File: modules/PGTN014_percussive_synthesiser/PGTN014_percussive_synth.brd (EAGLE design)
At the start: 78.9 x 100.4 mm, 201 parts, among them IC1 LM13700N, IC2 LM13700N, IC3 LM13700N, IC4 4046N, IC5 XR-2206, IC6 TL074P, Q1 2N3904, Q10 2N3906, Q11 2N3906, Q12 2N3906, Q13 2N3906, Q14 2N3906, Q2 2N3904, Q3 2N3904, Q4 2N3904, Q5 2N3904, Q6 2N3904, Q7 2N3904, Q8 2N3906, Q9 2N3904

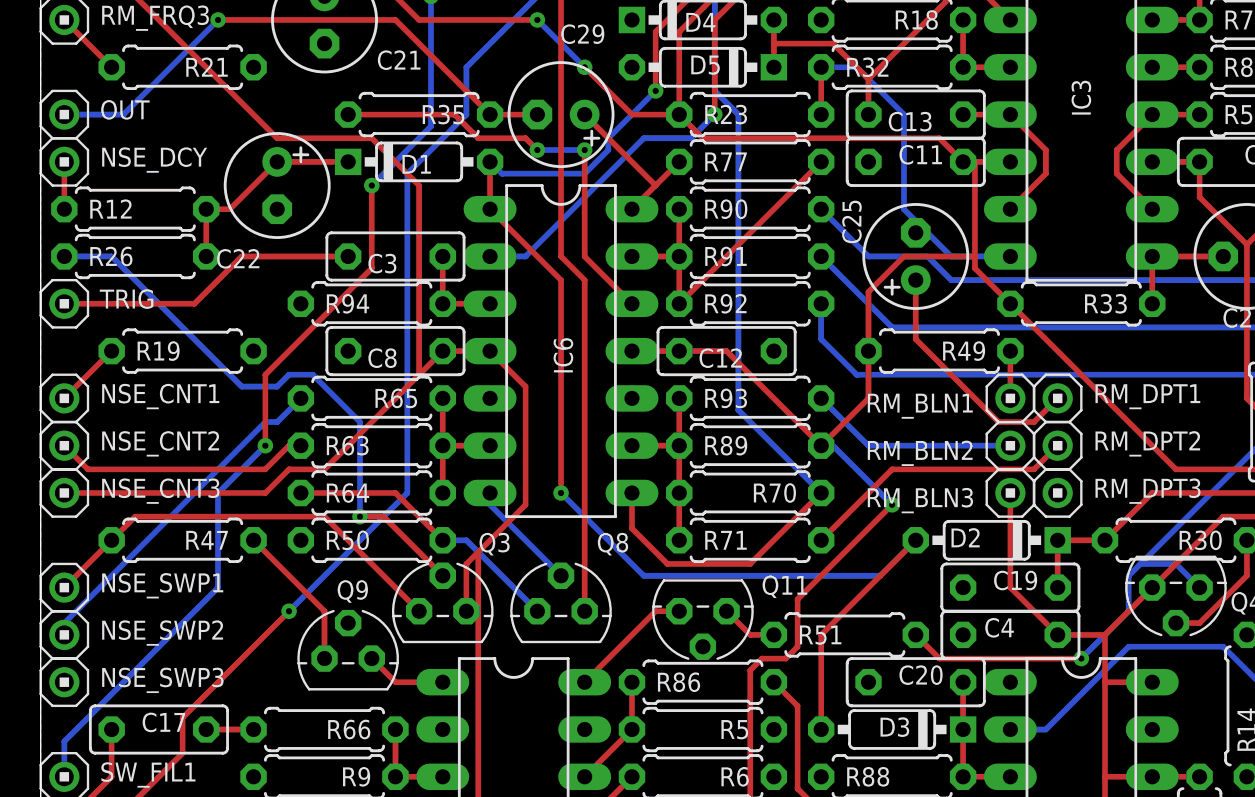
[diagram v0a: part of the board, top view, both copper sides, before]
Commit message: added sequencer
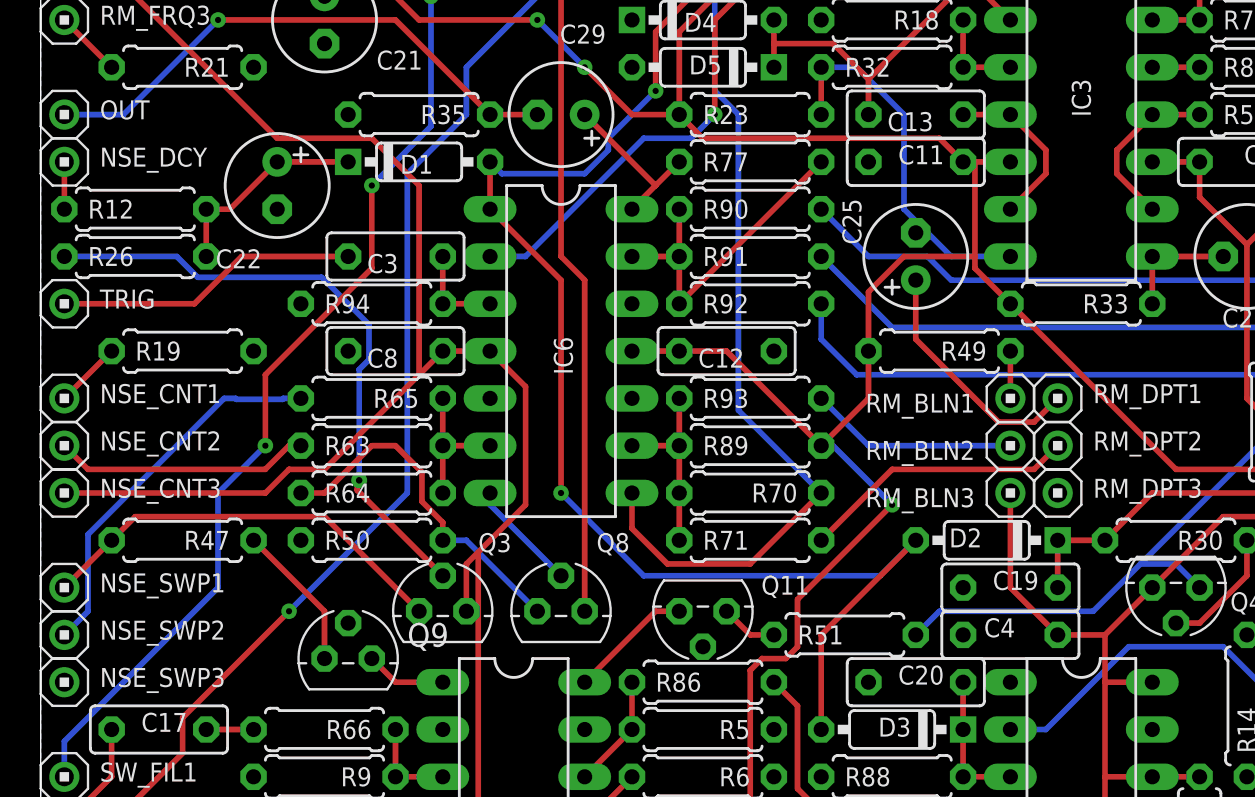
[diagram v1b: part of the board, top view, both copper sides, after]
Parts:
- Q9: value 2N3904 -> 2N3906
- R16: value 10k -> 1k
- R35: value 20k -> 10k
- R36: value (none) -> 10k
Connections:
- removed net PE: IC6.12, R35.2
- net GND: now also IC6.12, R35.2
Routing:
- net PE: track 22.8 -> 0.00 mm, vias 2 -> 0
- net N$15: track 15.3 -> 18.9 mm
- net N$10: track 30.9 -> 33.7 mm
- net N$45: track 41.6 -> 39.4 mm, vias 1 -> 0
- net N$13: track 18.3 -> 20.4 mm

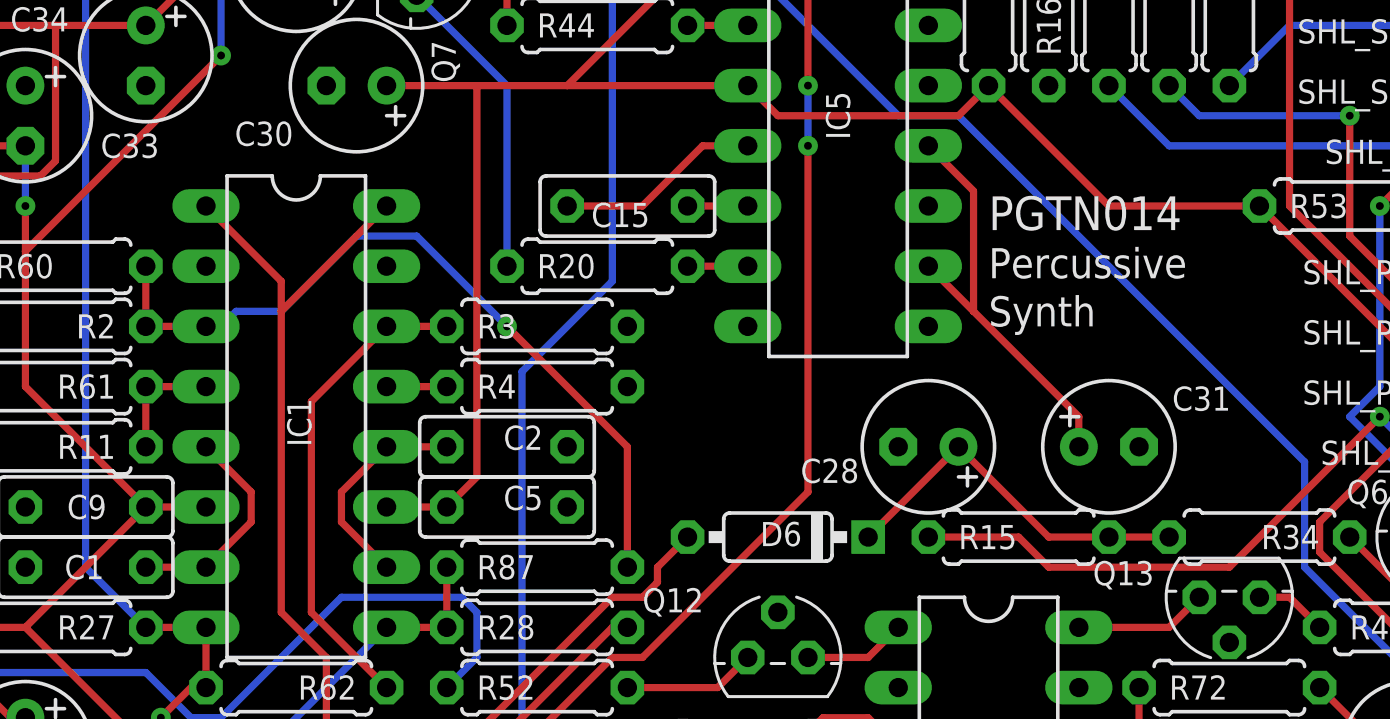
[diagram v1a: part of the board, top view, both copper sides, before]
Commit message: Fix for following issues * Pin 12 of IC5 shorted to pin 10. Pin 12 should be GND, but not pin 10 so have to kludge on IC pin. * SHL_SWP3 should connect to GND. No big deal as can just connect pot directly to GND instead. * Pin 12 of IC6 not connected to GND. * Pin 3 and 4 of IC1 swapped.
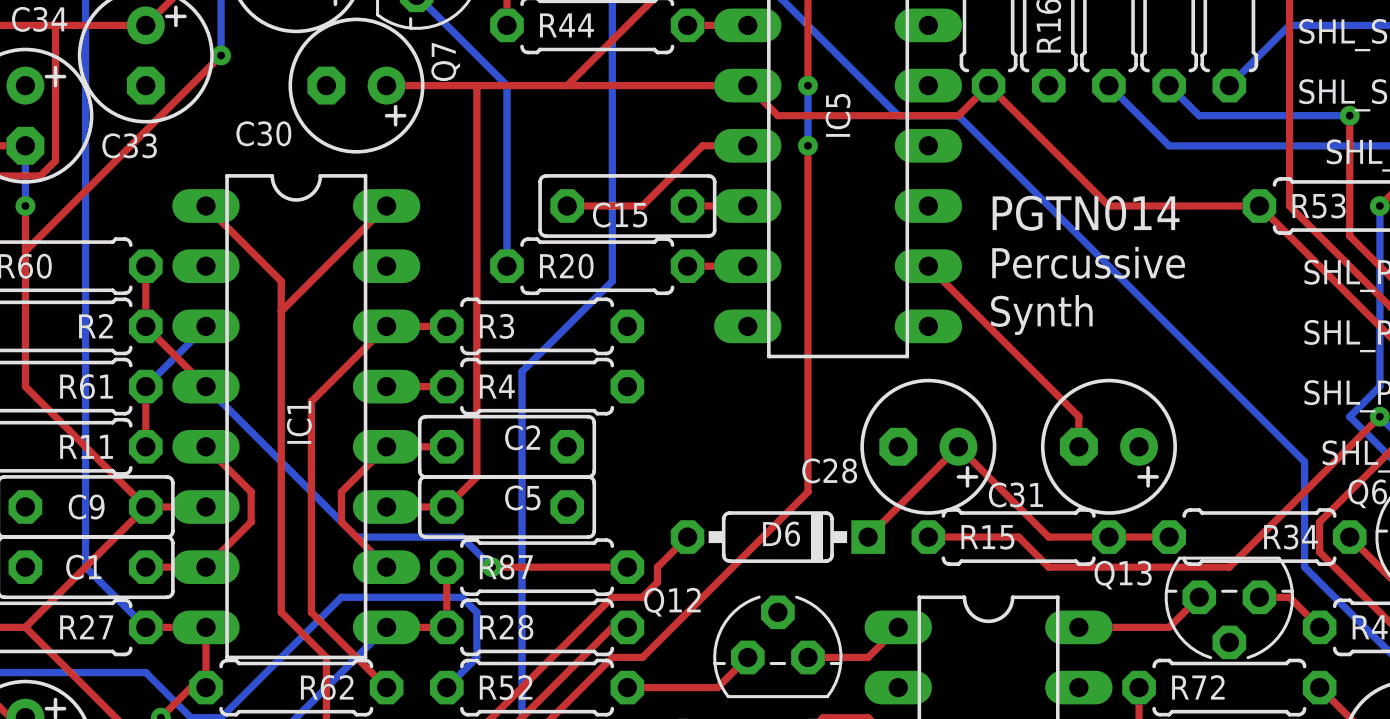
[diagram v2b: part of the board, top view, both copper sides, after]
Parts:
- turned C31 to 180 degrees
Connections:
- removed net N$105: C31.+, IC5.10, IC5.12
- removed net N$70: SHL_SWP3.1
- new net N$113: C31.-, IC5.10
- net GND: now also C31.+, IC5.12, SHL_SWP3.1; no longer C31.-
- net N$25: now also IC1.3; no longer IC1.4
- net N$30: now also IC1.4; no longer IC1.3
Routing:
- net N$105: track 18.0 -> 0.00 mm
- net N$113: track 0.00 -> 10.3 mm
- net N$30: track 33.2 -> 27.1 mm
- net N$25: track 5.08 -> 6.13 mm
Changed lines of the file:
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@@
 <attribute name="VALUE" x="37.211" y="74.676" size="1.016" layer="27" font="vector" ratio="15"/>
 </element>
-<element name="C31" library="capacitors" package="E2,5-6" value="10uF" x="60.96" y="67.31" smashed="yes">
-<attribute name="NAME" x="63.627" y="68.834" size="1.016" layer="25" font="vector" ratio="15"/>
-<attribute name="SPICEPREFIX" value="C" x="60.96" y="67.31" size="1.778" layer="27" display="off"/>
-<attribute name="VALUE" x="63.627" y="64.643" size="1.016" layer="27" font="vector" ratio="15"/>
+<element name="C31" library="capacitors" package="E2,5-6" value="10uF" x="60.96" y="67.31" smashed="yes" rot="R180">
+<attribute name="NAME" x="58.293" y="65.786" size="1.016" layer="25" font="vector" ratio="15" rot="R180"/>
+<attribute name="SPICEPREFIX" value="C" x="60.96" y="67.31" size="1.778" layer="27" rot="R180" display="off"/>
+<attribute name="VALUE" x="58.293" y="69.977" size="1.016" layer="27" font="vector" ratio="15" rot="R180"/>
 </element>
 <element name="IMP_OUT" library="connectors" package="HEADER/MALE/01" value="HEADER/MALE/01" x="41.91" y="1.27" smashed="yes">
@@
 <contactref element="C32" pad="-"/>
 <contactref element="C30" pad="-"/>
-<contactref element="C31" pad="-"/>
 <contactref element="C5" pad="1"/>
 <contactref element="C9" pad="2"/>
@@
 <contactref element="IC6" pad="12"/>
 <contactref element="R35" pad="2"/>
+<contactref element="SHL_SWP3" pad="1"/>
+<contactref element="IC5" pad="12"/>
+<contactref element="C31" pad="+"/>
 </signal>
 <signal name="+12V">
@@
 </signal>
 <signal name="N$18">
-<contactref element="IC1" pad="1"/>
 <contactref element="Q8" pad="1"/>
 <contactref element="IC1" pad="16"/>
@@
 <wire x1="26.035" y1="74.295" x2="26.035" y2="73.025" width="0.3048" layer="1"/>
 <wire x1="26.035" y1="73.025" x2="26.035" y2="60.325" width="0.3048" layer="1"/>
-<wire x1="22.86" y1="77.47" x2="26.035" y2="74.295" width="0.3048" layer="1"/>
 <wire x1="26.035" y1="73.025" x2="30.48" y2="77.47" width="0.3048" layer="1"/>
+<contactref element="IC1" pad="1"/>
+<wire x1="26.035" y1="74.295" x2="22.86" y2="77.47" width="0.3048" layer="1"/>
 </signal>
 <signal name="N$19">
-<contactref element="IC1" pad="5"/>
 <contactref element="IC1" pad="7"/>
 <contactref element="C1" pad="2"/>
 <wire x1="22.86" y1="62.23" x2="20.32" y2="62.23" width="0.3048" layer="1"/>
-<wire x1="24.765" y1="65.405" x2="22.86" y2="67.31" width="0.3048" layer="1"/>
 <wire x1="24.765" y1="64.135" x2="24.765" y2="65.405" width="0.3048" layer="1"/>
 <wire x1="22.86" y1="62.23" x2="24.765" y2="64.135" width="0.3048" layer="1"/>
+<contactref element="IC1" pad="5"/>
+<wire x1="24.765" y1="65.405" x2="22.86" y2="67.31" width="0.3048" layer="1"/>
 </signal>
 <signal name="N$20">
@@
 <signal name="N$25">
 <contactref element="R61" pad="1"/>
-<contactref element="IC1" pad="4"/>
 <contactref element="R11" pad="1"/>
 <wire x1="20.32" y1="69.85" x2="20.32" y2="67.31" width="0.3048" layer="1"/>
-<wire x1="20.32" y1="69.85" x2="22.86" y2="69.85" width="0.3048" layer="1"/>
+<contactref element="IC1" pad="3"/>
+<wire x1="20.32" y1="69.85" x2="22.86" y2="72.39" width="0.3048" layer="16"/>
 </signal>
 <signal name="N$26">
@@
 </signal>
 <signal name="N$30">
-<contactref element="IC1" pad="3"/>
 <contactref element="R87" pad="2"/>
 <contactref element="R2" pad="1"/>
 <contactref element="R60" pad="2"/>
 <wire x1="20.32" y1="74.93" x2="20.32" y2="72.39" width="0.3048" layer="1"/>
-<wire x1="20.32" y1="72.39" x2="22.86" y2="72.39" width="0.3048" layer="1"/>
-<wire x1="40.64" y1="67.31" x2="40.64" y2="62.23" width="0.3048" layer="1"/>
-<wire x1="35.56" y1="72.39" x2="40.64" y2="67.31" width="0.3048" layer="1"/>
-<wire x1="31.75" y1="76.2" x2="35.56" y2="72.39" width="0.3048" layer="16"/>
-<wire x1="29.21" y1="76.2" x2="31.75" y2="76.2" width="0.3048" layer="16"/>
-<wire x1="26.035" y1="73.025" x2="29.21" y2="76.2" width="0.3048" layer="16"/>
-<wire x1="24.13" y1="73.025" x2="26.035" y2="73.025" width="0.3048" layer="16"/>
-<wire x1="23.495" y1="72.39" x2="24.13" y2="73.025" width="0.3048" layer="16"/>
-<wire x1="22.86" y1="72.39" x2="23.495" y2="72.39" width="0.3048" layer="16"/>
-<via x="35.56" y="72.39" extent="1-16" drill="0.3302"/>
+<contactref element="IC1" pad="4"/>
+<wire x1="34.925" y1="62.23" x2="40.64" y2="62.23" width="0.3048" layer="1"/>
+<wire x1="33.655" y1="63.5" x2="34.925" y2="62.23" width="0.3048" layer="16"/>
+<wire x1="29.21" y1="63.5" x2="33.655" y2="63.5" width="0.3048" layer="16"/>
+<wire x1="22.86" y1="69.85" x2="29.21" y2="63.5" width="0.3048" layer="16"/>
+<wire x1="22.86" y1="69.85" x2="20.32" y2="72.39" width="0.3048" layer="1"/>
+<via x="34.925" y="62.23" extent="1-16" drill="0.3302"/>
 </signal>
 <signal name="N$31">
@@
 <via x="72.39" y="77.47" extent="1-16" drill="0.3302"/>
 </signal>
-<signal name="N$70">
-<contactref element="SHL_SWP3" pad="1"/>
-</signal>
 <signal name="N$71">
 <contactref element="SHL_SWP2" pad="1"/>
@@
 <wire x1="45.72" y1="77.47" x2="43.18" y2="77.47" width="0.3048" layer="1"/>
 </signal>
-<signal name="N$105">
-<contactref element="IC5" pad="10"/>
-<contactref element="C31" pad="+"/>
-<contactref element="IC5" pad="12"/>
-<wire x1="59.69" y1="68.58" x2="55.245" y2="73.025" width="0.3048" layer="1"/>
-<wire x1="55.245" y1="73.025" x2="53.34" y2="74.93" width="0.3048" layer="1"/>
-<wire x1="59.69" y1="67.31" x2="59.69" y2="68.58" width="0.3048" layer="1"/>
-<wire x1="55.245" y1="78.105" x2="53.34" y2="80.01" width="0.3048" layer="1"/>
-<wire x1="55.245" y1="73.025" x2="55.245" y2="78.105" width="0.3048" layer="1"/>
-</signal>
 <signal name="N$107">
 <contactref element="SHL_OUT" pad="1"/>
@@
 <via x="9.525" y="54.61" extent="1-16" drill="0.3302"/>
 </signal>
+<signal name="N$113">
+<contactref element="IC5" pad="10"/>
+<contactref element="C31" pad="-"/>
+<wire x1="53.34" y1="74.93" x2="59.69" y2="68.58" width="0.3048" layer="1"/>
+<wire x1="59.69" y1="68.58" x2="59.69" y2="67.31" width="0.3048" layer="1"/>
+</signal>
 </signals>
